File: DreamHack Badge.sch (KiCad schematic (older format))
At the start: 26 parts, among them J1 USB_B_Mini, J2 Conn_01x14_Female, J4 Conn_01x04_Female, U1 ESP32-WROOM-32, U2 AMS1117-3.3, U3 AMS1117-5.0, U4 MCP73831-2-OT

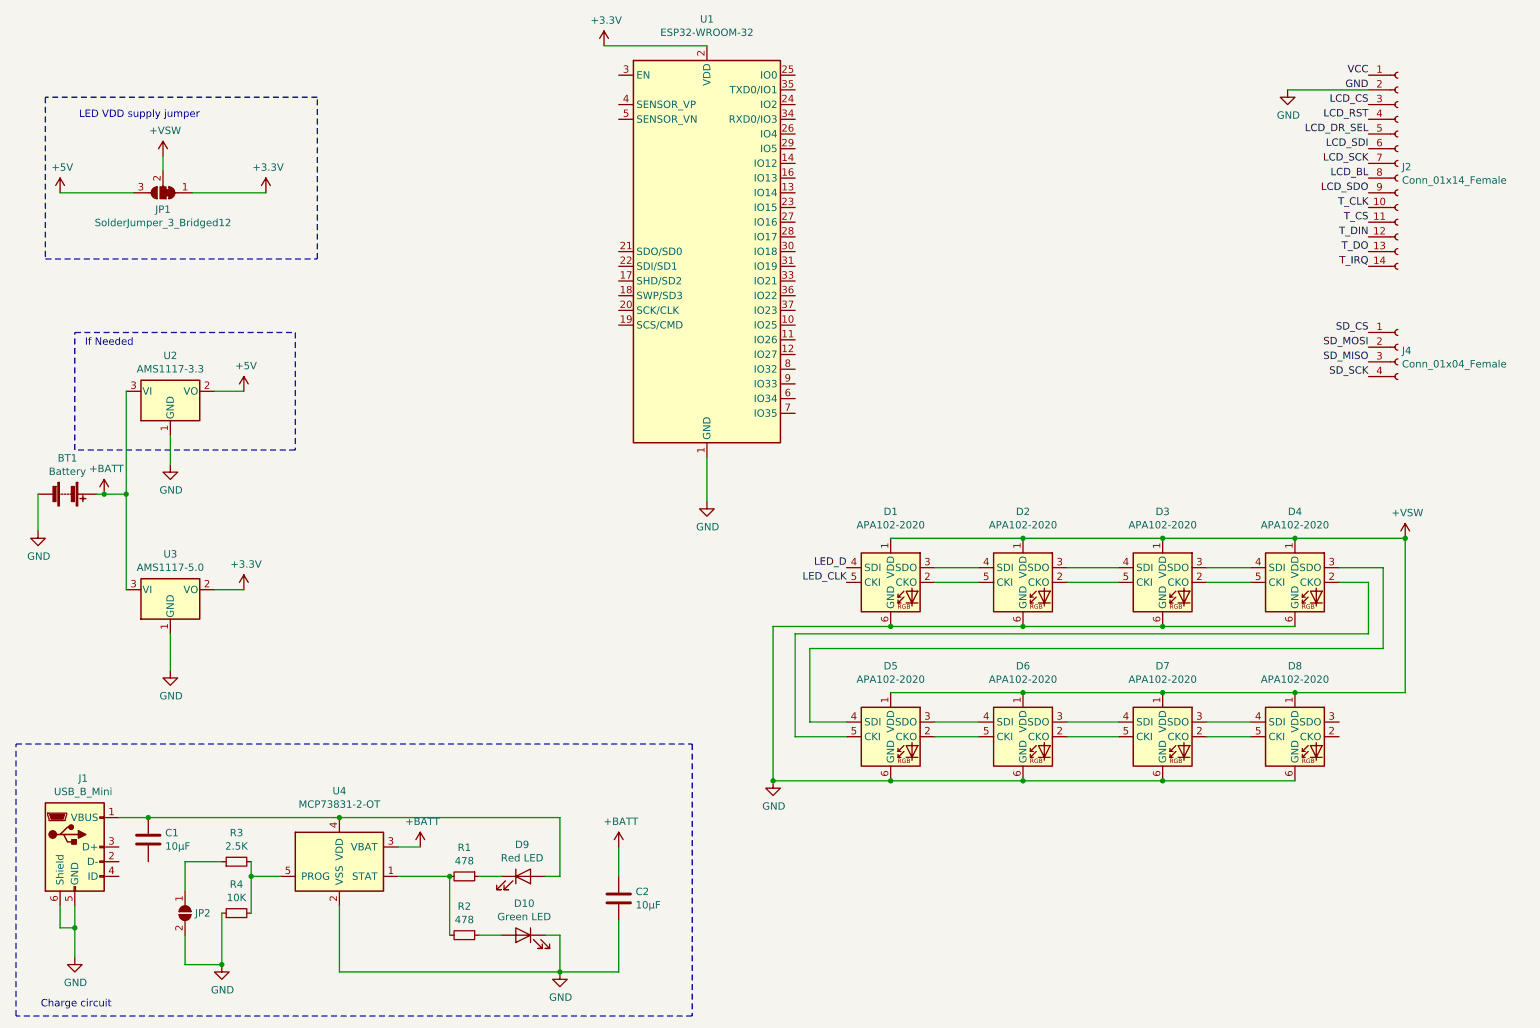
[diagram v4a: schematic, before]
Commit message: added ch340 usb to serial for direct flshing
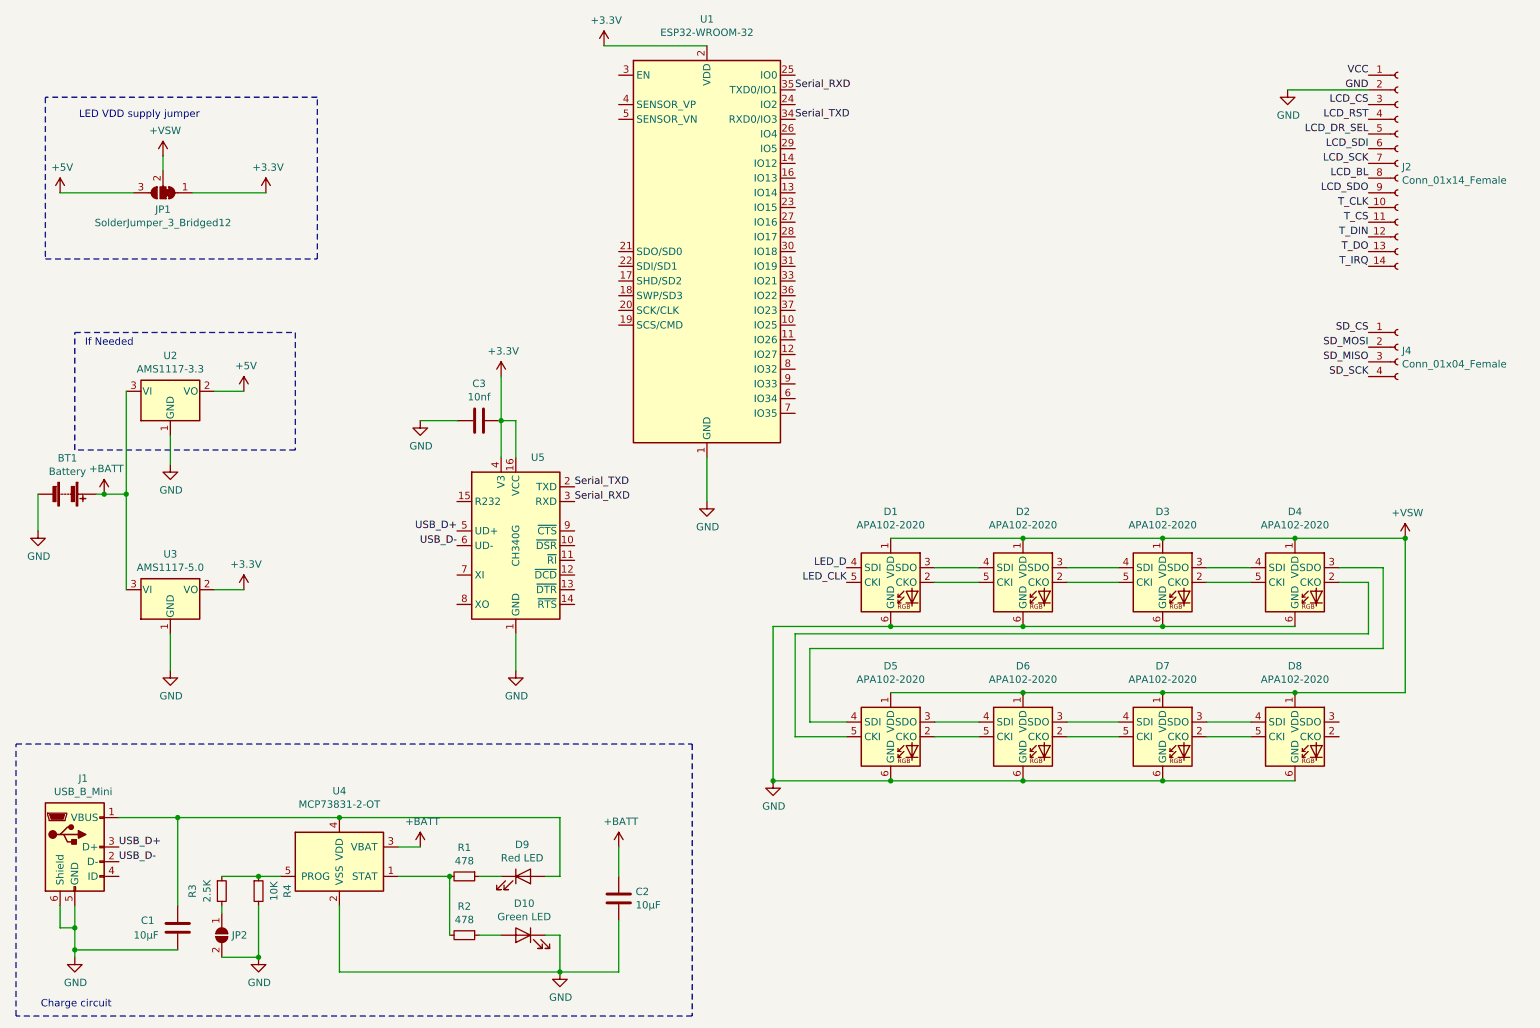
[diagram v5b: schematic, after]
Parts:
- added C3: 10nf, Capacitors_SMD:C_0805_HandSoldering, symbol Device:C
- added U5: CH340G, Package_SO:SOIC-16_3.9x9.9mm_P1.27mm, symbol Interface_USB:CH340G
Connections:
- net +3V3: now also C3.1, U5.16 (VCC), U5.4 (V3)
- net GND: now also C1.2, R4.2, C3.2, U5.1 (GND); no longer R4.1
- net Serial_TXD: now reaches U1.34 (RXD0/IO3)
- net Serial_TXD: now also U5.2 (TXD)
- net Serial_RXD: now reaches U1.35 (TXD0/IO1)
- net Serial_RXD: now also U5.3 (RXD)
- net USB_D-: now reaches J1.2 (D-)
- net USB_D-: now also U5.6 (UD-)
- net USB_D+: now reaches J1.3 (D+)
- net USB_D+: now also U5.5 (UD+)
- net at R3.1: now also R4.1, U4.5 (PROG); no longer JP2.1 (A)
- new net: JP2.1 (A), R3.2
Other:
- moved on the sheet: C1, JP2, R3, R4
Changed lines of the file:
@@
 	5300 850  4600 850
 Wire Wire Line
-	1000 7050 1000 6850
+	1000 7050 1000 7000
 Wire Wire Line
 	900  6700 900  6850
@@
 	1    0    0    -1
 $EndComp
-Wire Wire Line
-	1300 6100 1500 6100
 $Comp
 L Device:LED D9
@@
 Connection ~ 2800 6100
 $Comp
-L power:GND #PWR0114
-U 1 1 5D05F7A6
-P 2000 7100
-F 0 "#PWR0114" H 2000 6850 50  0001 C CNN
-F 1 "GND" H 2005 6927 50  0000 C CNN
-F 2 "" H 2000 7100 50  0001 C CNN
-F 3 "" H 2000 7100 50  0001 C CNN
-	1    2000 7100
-	1    0    0    -1
-$EndComp
-$Comp
-L Device:R_Small R3
-U 1 1 5D05F7DF
-P 2100 6400
-F 0 "R3" V 2296 6400 50  0000 C CNN
-F 1 "2.5K" V 2205 6400 50  0000 C CNN
-F 2 "Resistors_SMD:R_0805_HandSoldering" H 2100 6400 50  0001 C CNN
-F 3 "~" H 2100 6400 50  0001 C CNN
-	1    2100 6400
-	0    -1   -1   0
-$EndComp
-$Comp
 L Device:R_Small R4
 U 1 1 5D05FD79
-P 2100 6750
-F 0 "R4" V 2296 6750 50  0000 C CNN
-F 1 "10K" V 2205 6750 50  0000 C CNN
-F 2 "Resistors_SMD:R_0805_HandSoldering" H 2100 6750 50  0001 C CNN
-F 3 "~" H 2100 6750 50  0001 C CNN
-	1    2100 6750
-	0    -1   -1   0
-$EndComp
-Wire Wire Line
-	2200 6400 2200 6500
-Wire Wire Line
-	2400 6500 2200 6500
-Connection ~ 2200 6500
-Wire Wire Line
-	2200 6500 2200 6750
-Wire Wire Line
-	2000 6400 1750 6400
-Wire Wire Line
-	1750 7100 2000 7100
-Wire Wire Line
-	2000 6750 2000 7100
-Connection ~ 2000 7100
-$Comp
-L Jumper:SolderJumper_2_Open JP2
-U 1 1 5D07C461
-P 1750 6750
-F 0 "JP2" V 1750 6818 50  0000 L CNN
-F 1 "SolderJumper_2_Open" V 1795 6818 50  0001 L CNN
-F 2 "Jumper:SolderJumper-2_P1.3mm_Open_RoundedPad1.0x1.5mm" H 1750 6750 50  0001 C CNN
-F 3 "~" H 1750 6750 50  0001 C CNN
-	1    1750 6750
-	0    1    1    0
-$EndComp
-Wire Wire Line
-	1750 6400 1750 6600
-Wire Wire Line
-	1750 6900 1750 7100
+P 2250 6600
+F 0 "R4" V 2446 6600 50  0000 C CNN
+F 1 "10K" V 2355 6600 50  0000 C CNN
+F 2 "Resistors_SMD:R_0805_HandSoldering" H 2250 6600 50  0001 C CNN
+F 3 "~" H 2250 6600 50  0001 C CNN
+	1    2250 6600
+	1    0    0    -1
+$EndComp
 $Comp
 L Device:C C1
 U 1 1 5D081D2A
-P 1500 6250
-F 0 "C1" H 1615 6296 50  0000 L CNN
-F 1 "10μF" H 1615 6205 50  0000 L CNN
-F 2 "Capacitors_SMD:C_0805_HandSoldering" H 1538 6100 50  0001 C CNN
-F 3 "~" H 1500 6250 50  0001 C CNN
-	1    1500 6250
-	1    0    0    -1
-$EndComp
-Connection ~ 1500 6100
-Wire Wire Line
-	1500 6100 2800 6100
+P 1700 6850
+F 0 "C1" H 1450 6900 50  0000 L CNN
+F 1 "10μF" H 1400 6800 50  0000 L CNN
+F 2 "Capacitors_SMD:C_0805_HandSoldering" H 1738 6700 50  0001 C CNN
+F 3 "~" H 1700 6850 50  0001 C CNN
+	1    1700 6850
+	1    0    0    -1
+$EndComp
 $Comp
 L Device:C C2
@@
 Text Notes 1400 2900 2    50   ~ 0
 If Needed
+Text Label 1300 6300 0    50   ~ 0
+USB_D+
+Text Label 1300 6400 0    50   ~ 0
+USB_D-
+Wire Wire Line
+	1300 6100 1700 6100
+$Comp
+L Jumper:SolderJumper_2_Open JP2
+U 1 1 5D07C461
+P 2000 6900
+F 0 "JP2" V 2000 6968 50  0000 L CNN
+F 1 "SolderJumper_2_Open" V 2045 6968 50  0001 L CNN
+F 2 "Jumper:SolderJumper-2_P1.3mm_Open_RoundedPad1.0x1.5mm" H 2000 6900 50  0001 C CNN
+F 3 "~" H 2000 6900 50  0001 C CNN
+	1    2000 6900
+	0    1    1    0
+$EndComp
+$Comp
+L Device:R_Small R3
+U 1 1 5D05F7DF
+P 2000 6600
+F 0 "R3" V 1800 6600 50  0000 C CNN
+F 1 "2.5K" V 1900 6600 50  0000 C CNN
+F 2 "Resistors_SMD:R_0805_HandSoldering" H 2000 6600 50  0001 C CNN
+F 3 "~" H 2000 6600 50  0001 C CNN
+	1    2000 6600
+	1    0    0    -1
+$EndComp
+$Comp
+L power:GND #PWR0114
+U 1 1 5D05F7A6
+P 2250 7050
+F 0 "#PWR0114" H 2250 6800 50  0001 C CNN
+F 1 "GND" H 2255 6877 50  0000 C CNN
+F 2 "" H 2250 7050 50  0001 C CNN
+F 3 "" H 2250 7050 50  0001 C CNN
+	1    2250 7050
+	1    0    0    -1
+$EndComp
+Wire Wire Line
+	2400 6500 2250 6500
+Connection ~ 2250 6500
+Wire Wire Line
+	2250 6500 2000 6500
+Wire Wire Line
+	2000 6700 2000 6750
+Wire Wire Line
+	2250 6700 2250 7050
+Wire Wire Line
+	2000 7050 2250 7050
+Connection ~ 2250 7050
+Wire Wire Line
+	1700 6100 1700 6700
+Connection ~ 1700 6100
+Wire Wire Line
+	1700 6100 2800 6100
+Wire Wire Line
+	1700 7000 1000 7000
+Connection ~ 1000 7000
+Wire Wire Line
+	1000 7000 1000 6850
+Text Label 3600 4150 2    50   ~ 0
+USB_D+
+Text Label 3600 4250 2    50   ~ 0
+USB_D-
+$Comp
+L power:GND #PWR?
+U 1 1 5D125AAC
+P 4000 5100
+F 0 "#PWR?" H 4000 4850 50  0001 C CNN
+F 1 "GND" H 4005 4927 50  0000 C CNN
+F 2 "" H 4000 5100 50  0001 C CNN
+F 3 "" H 4000 5100 50  0001 C CNN
+	1    4000 5100
+	1    0    0    -1
+$EndComp
+Wire Wire Line
+	4000 4850 4000 5100
+$Comp
+L Device:C C3
+U 1 1 5D1291F4
+P 3750 3400
+F 0 "C3" V 3498 3400 50  0000 C CNN
+F 1 "10nf" V 3589 3400 50  0000 C CNN
+F 2 "Capacitors_SMD:C_0805_HandSoldering" H 3788 3250 50  0001 C CNN
+F 3 "~" H 3750 3400 50  0001 C CNN
+	1    3750 3400
+	0    1    1    0
+$EndComp
+$Comp
+L Interface_USB:CH340G U5
+U 1 1 5D134902
+P 4000 4250
+F 0 "U5" H 4150 4850 50  0000 C CNN
+F 1 "CH340G" V 4000 4250 50  0000 C CNN
+F 2 "Package_SO:SOIC-16_3.9x9.9mm_P1.27mm" H 4050 3700 50  0001 L CNN
+F 3 "http://www.datasheet5.com/pdf-local-2195953" H 3650 5050 50  0001 C CNN
+	1    4000 4250
+	1    0    0    -1
+$EndComp
+$Comp
+L power:+3.3V #PWR?
+U 1 1 5D137571
+P 3900 3100
+F 0 "#PWR?" H 3900 2950 50  0001 C CNN
+F 1 "+3.3V" H 3915 3273 50  0000 C CNN
+F 2 "" H 3900 3100 50  0001 C CNN
+F 3 "" H 3900 3100 50  0001 C CNN
+	1    3900 3100
+	1    0    0    -1
+$EndComp
+Wire Wire Line
+	3900 3100 3900 3400
+Connection ~ 3900 3400
+Wire Wire Line
+	3900 3400 3900 3650
+Wire Wire Line
+	3900 3400 4000 3400
+Wire Wire Line
+	4000 3400 4000 3650
+$Comp
+L power:GND #PWR?
+U 1 1 5D141509
+P 3350 3400
+F 0 "#PWR?" H 3350 3150 50  0001 C CNN
+F 1 "GND" H 3355 3227 50  0000 C CNN
+F 2 "" H 3350 3400 50  0001 C CNN
+F 3 "" H 3350 3400 50  0001 C CNN
+	1    3350 3400
+	1    0    0    -1
+$EndComp
+Wire Wire Line
+	3350 3400 3600 3400
+Text Label 4400 3850 0    50   ~ 0
+Serial_TXD
+Text Label 4400 3950 0    50   ~ 0
+Serial_RXD
+Text Label 5900 1150 0    50   ~ 0
+Serial_RXD
+Text Label 5900 1350 0    50   ~ 0
+Serial_TXD
 $EndSCHEMATC
